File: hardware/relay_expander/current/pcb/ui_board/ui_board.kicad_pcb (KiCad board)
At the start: 2 copper layers, 84 x 26 mm, 4 parts, among them J1 Conn_01x20_Socket

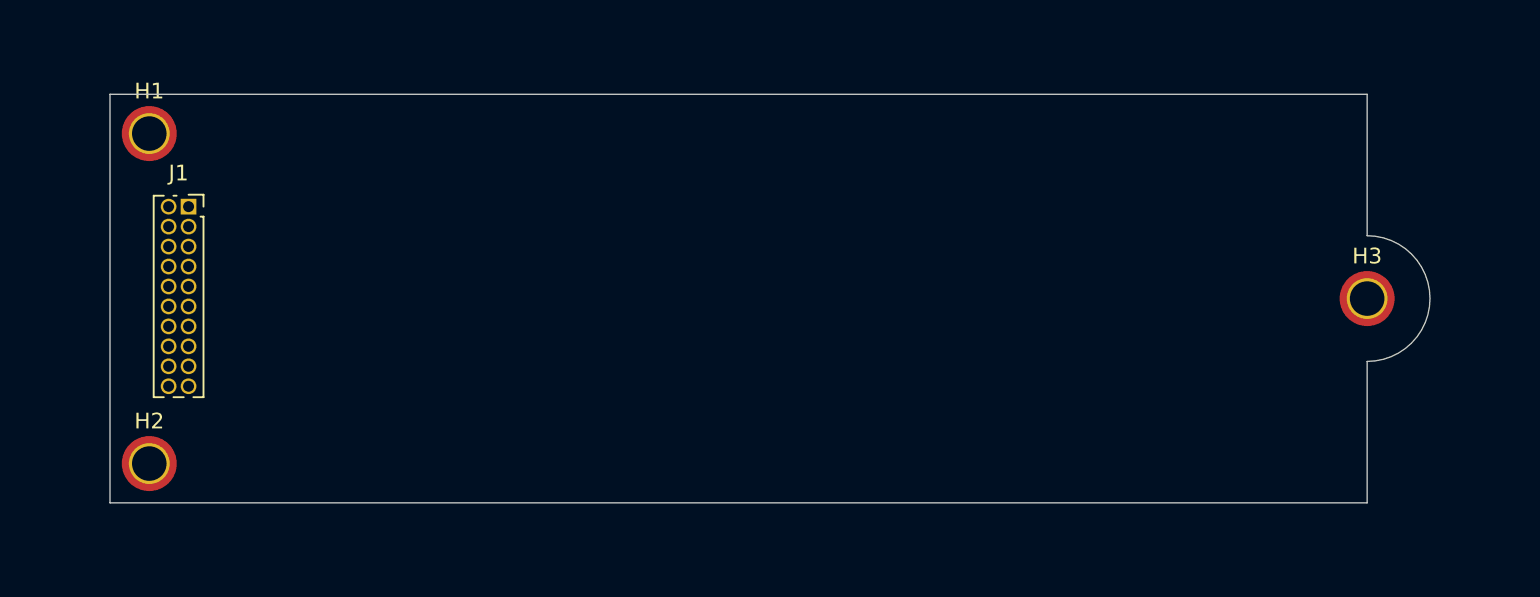
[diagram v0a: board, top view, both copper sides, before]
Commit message: [ADD] ui-board for relay - basic layout
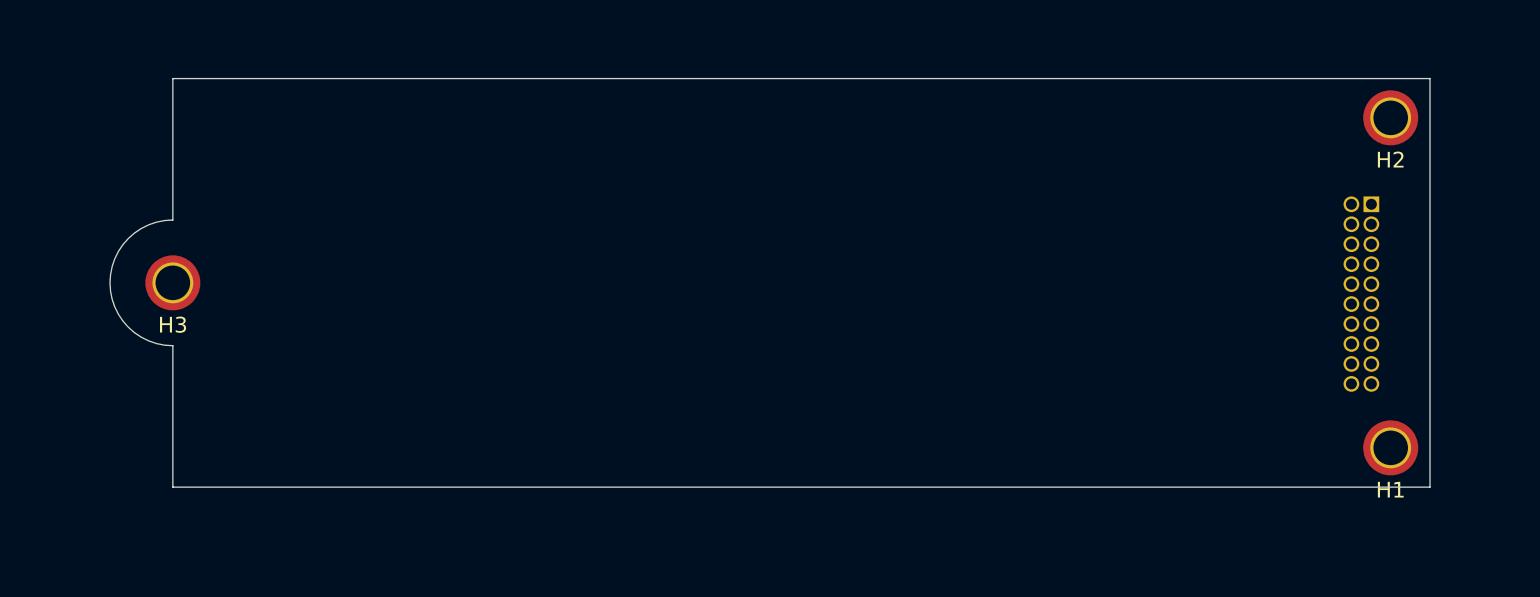
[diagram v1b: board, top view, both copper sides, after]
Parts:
- J1: footprint Connector_PinSocket_1.27mm:PinSocket_2x10_P1.27mm_Vertical -> homeautomation_core:PinSocket_2x10_P1.27mm_Vertical_Bottom; moved to B.Cu
- moved H2 82.0 mm to (181.5, 88.5), turned to 180 degrees
- moved H1 81.5 mm to (181.5, 109.5), turned to 180 degrees
- moved H3 76.0 mm to (104.0, 99.0), turned to 180 degrees
- moved J1 74.0 mm to (179.0, 94.0), turned to 180 degrees
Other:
- outline, holes or cut-outs redrawn

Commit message: [ADD] ui_board finished setup]
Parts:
- added D1: LED, LED_SMD:LED_1206_3216Metric_Pad1.42x1.75mm_HandSolder, F.Cu at (116.5, 93.0)
- added D10: LED, LED_SMD:LED_1206_3216Metric_Pad1.42x1.75mm_HandSolder, F.Cu at (124.0, 104.0)
- added D11: LED, LED_SMD:LED_1206_3216Metric_Pad1.42x1.75mm_HandSolder, F.Cu at (131.5, 104.0)
- added D12: LED, LED_SMD:LED_1206_3216Metric_Pad1.42x1.75mm_HandSolder, F.Cu at (139.0, 104.0)
- added D13: LED, LED_SMD:LED_1206_3216Metric_Pad1.42x1.75mm_HandSolder, F.Cu at (146.5, 104.0)
- added D14: LED, LED_SMD:LED_1206_3216Metric_Pad1.42x1.75mm_HandSolder, F.Cu at (154.0, 104.0)
- added D15: LED, LED_SMD:LED_1206_3216Metric_Pad1.42x1.75mm_HandSolder, F.Cu at (161.5, 104.0)
- added D16: LED, LED_SMD:LED_1206_3216Metric_Pad1.42x1.75mm_HandSolder, F.Cu at (169.0, 104.0)
- added D2: LED, LED_SMD:LED_1206_3216Metric_Pad1.42x1.75mm_HandSolder, F.Cu at (124.0, 93.0)
- added D3: LED, LED_SMD:LED_1206_3216Metric_Pad1.42x1.75mm_HandSolder, F.Cu at (131.5, 93.0)
- added D4: LED, LED_SMD:LED_1206_3216Metric_Pad1.42x1.75mm_HandSolder, F.Cu at (139.0, 93.0)
- added D5: LED, LED_SMD:LED_1206_3216Metric_Pad1.42x1.75mm_HandSolder, F.Cu at (146.5, 93.0)
- added D6: LED, LED_SMD:LED_1206_3216Metric_Pad1.42x1.75mm_HandSolder, F.Cu at (154.0, 93.0)
- added D7: LED, LED_SMD:LED_1206_3216Metric_Pad1.42x1.75mm_HandSolder, F.Cu at (161.5, 93.0)
- added D8: LED, LED_SMD:LED_1206_3216Metric_Pad1.42x1.75mm_HandSolder, F.Cu at (169.0, 93.0)
- added D9: LED, LED_SMD:LED_1206_3216Metric_Pad1.42x1.75mm_HandSolder, F.Cu at (116.5, 104.0)
- added R1: 1k, Resistor_SMD:R_1206_3216Metric_Pad1.30x1.75mm_HandSolder, B.Cu at (114.0, 90.5)
- added R10: R330, Resistor_SMD:R_1206_3216Metric_Pad1.30x1.75mm_HandSolder, B.Cu at (126.5, 107.5)
- added R11: R330, Resistor_SMD:R_1206_3216Metric_Pad1.30x1.75mm_HandSolder, B.Cu at (134.0, 107.5)
- added R12: R330, Resistor_SMD:R_1206_3216Metric_Pad1.30x1.75mm_HandSolder, B.Cu at (141.5, 107.5)
- added R13: R330, Resistor_SMD:R_1206_3216Metric_Pad1.30x1.75mm_HandSolder, B.Cu at (149.0, 107.5)
- added R14: R330, Resistor_SMD:R_1206_3216Metric_Pad1.30x1.75mm_HandSolder, B.Cu at (156.5, 107.5)
- added R15: R330, Resistor_SMD:R_1206_3216Metric_Pad1.30x1.75mm_HandSolder, B.Cu at (164.0, 107.5)
- added R16: R330, Resistor_SMD:R_1206_3216Metric_Pad1.30x1.75mm_HandSolder, B.Cu at (171.5, 107.5)
- added R2: 1k, Resistor_SMD:R_1206_3216Metric_Pad1.30x1.75mm_HandSolder, B.Cu at (121.5, 90.5)
- added R3: 1k, Resistor_SMD:R_1206_3216Metric_Pad1.30x1.75mm_HandSolder, B.Cu at (129.0, 90.5)
- added R4: 1k, Resistor_SMD:R_1206_3216Metric_Pad1.30x1.75mm_HandSolder, B.Cu at (136.5, 90.5)
- added R5: 1k, Resistor_SMD:R_1206_3216Metric_Pad1.30x1.75mm_HandSolder, B.Cu at (144.0, 90.5)
- added R6: 1k, Resistor_SMD:R_1206_3216Metric_Pad1.30x1.75mm_HandSolder, B.Cu at (151.5, 90.5)
- added R7: 1k, Resistor_SMD:R_1206_3216Metric_Pad1.30x1.75mm_HandSolder, B.Cu at (159.0, 90.5)
- added R8: 1k, Resistor_SMD:R_1206_3216Metric_Pad1.30x1.75mm_HandSolder, B.Cu at (166.5, 90.5)
- added R9: R330, Resistor_SMD:R_1206_3216Metric_Pad1.30x1.75mm_HandSolder, B.Cu at (119.0, 107.5)
- H1, H2, H3: moved to B.Cu
- J1: footprint homeautomation_core:PinSocket_2x10_P1.27mm_Vertical_Bottom -> Connector_PinSocket_1.27mm:PinSocket_2x10_P1.27mm_Vertical
- moved J1 5.10 mm to (180.0, 99.0)
- turned H1 to 0 degrees
- turned H2 to 0 degrees
- turned H3 to 0 degrees
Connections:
- J1 pad 10: unconnected-(J1-Pin_10-Pad10) -> Net-(D3-K)
- J1 pad 11: unconnected-(J1-Pin_11-Pad11) -> Net-(D2-K)
- J1 pad 12: unconnected-(J1-Pin_12-Pad12) -> Net-(D1-K)
- J1 pad 13: unconnected-(J1-Pin_13-Pad13) -> Net-(D9-K)
- J1 pad 14: unconnected-(J1-Pin_14-Pad14) -> Net-(D10-K)
- J1 pad 15: unconnected-(J1-Pin_15-Pad15) -> Net-(D11-K)
- J1 pad 16: unconnected-(J1-Pin_16-Pad16) -> Net-(D12-K)
- J1 pad 17: unconnected-(J1-Pin_17-Pad17) -> Net-(D13-K)
- J1 pad 18: unconnected-(J1-Pin_18-Pad18) -> Net-(D14-K)
- J1 pad 19: unconnected-(J1-Pin_19-Pad19) -> Net-(D15-K)
- J1 pad 20: unconnected-(J1-Pin_20-Pad20) -> Net-(D16-K)
- J1 pad 5: unconnected-(J1-Pin_5-Pad5) -> Net-(D8-K)
- J1 pad 6: unconnected-(J1-Pin_6-Pad6) -> Net-(D7-K)
- J1 pad 7: unconnected-(J1-Pin_7-Pad7) -> Net-(D6-K)
- J1 pad 8: unconnected-(J1-Pin_8-Pad8) -> Net-(D5-K)
- J1 pad 9: unconnected-(J1-Pin_9-Pad9) -> Net-(D4-K)
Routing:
- net Net-(D1-K): track 0.00 -> 76.6 mm
- net +3V3: track 0.00 -> 72.2 mm
- net +12V: track 0.00 -> 69.4 mm, vias 0 -> 1
- net Net-(D10-K): track 0.00 -> 68.6 mm
- net Net-(D9-K): track 0.00 -> 65.1 mm
- net Net-(D3-K): track 0.00 -> 59.7 mm, vias 0 -> 1
- net Net-(D2-K): track 0.00 -> 57.5 mm
- net Net-(D12-K): track 0.00 -> 50.8 mm
- net Net-(D11-K): track 0.00 -> 49.8 mm
- net Net-(D4-K): track 0.00 -> 42.0 mm
- net Net-(D5-K): track 0.00 -> 41.5 mm, vias 0 -> 1
- net Net-(D13-K): track 0.00 -> 34.5 mm
- net Net-(D14-K): track 0.00 -> 33.1 mm
- net Net-(D6-K): track 0.00 -> 26.5 mm
- net Net-(D7-K): track 0.00 -> 24.2 mm, vias 0 -> 1
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- added copper zone on B.Cu, net GND
- added copper zone on F.Cu, net GND
